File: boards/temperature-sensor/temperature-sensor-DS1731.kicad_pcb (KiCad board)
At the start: 2 copper layers, 20.3 x 17.3 mm, 8 parts, among them J1 CONN_01X04_MALE, M3 MountingHole_3.2mm_M3, U1 DS1731U

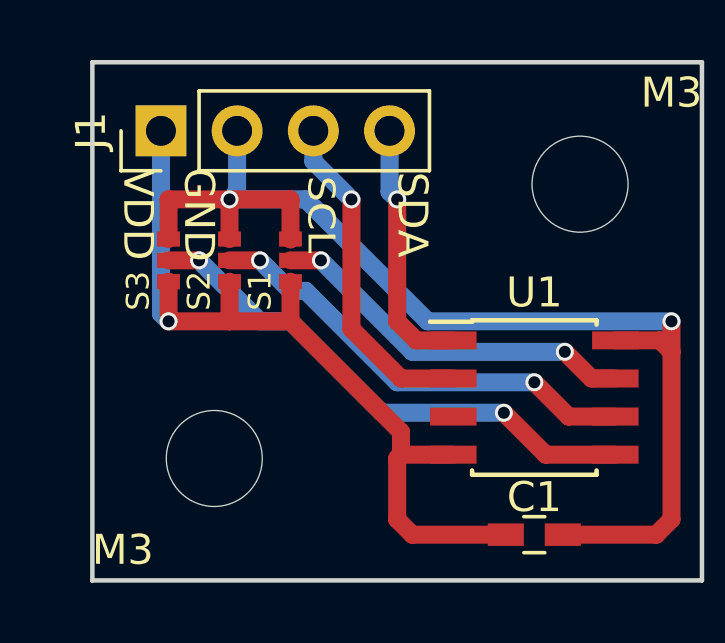
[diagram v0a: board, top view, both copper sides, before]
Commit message: boards/temperature_sensor: reduced number of vias, corrected spelling error
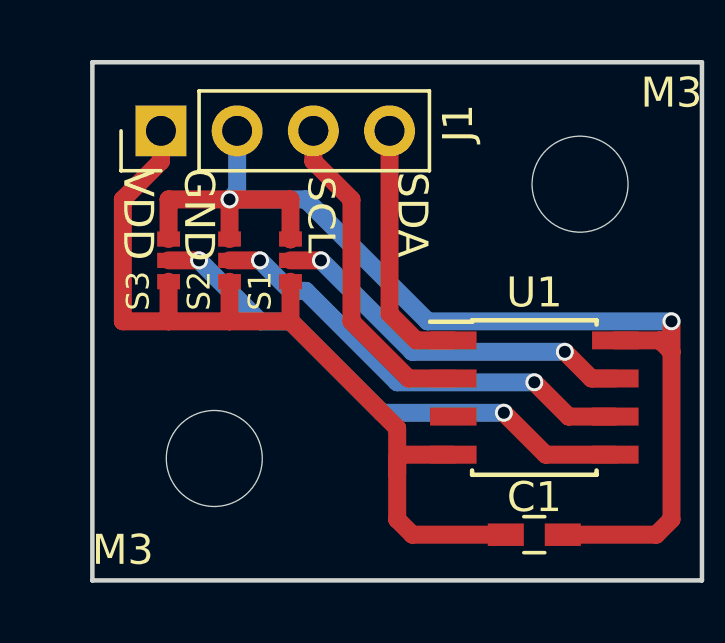
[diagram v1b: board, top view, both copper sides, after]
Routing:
- net /GND: track 28.2 -> 30.8 mm, vias 1 -> 0
- net /SCL: track 11.2 -> 11.1 mm, vias 1 -> 0
- net /SDA: vias 1 -> 0
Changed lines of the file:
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@@
     (thickness 1.6)
     (drawings 12)
-    (tracks 70)
+    (tracks 68)
     (zones 0)
     (modules 8)
@@
     (34 B.Paste user)
     (35 F.Paste user)
-    (36 B.SilkS user)
-    (37 F.SilkS user)
+    (36 B.SilkS user hide)
+    (37 F.SilkS user hide)
     (38 B.Mask user)
     (39 F.Mask user)
@@
     (descr "Through hole straight pin header, 1x04, 2.54mm pitch, single row")
     (tags "Through hole pin header THT 1x04 2.54mm single row")
-    (fp_text reference J1 (at 0 -2.33 90) (layer F.SilkS)
+    (fp_text reference J1 (at 0.254 9.906 90) (layer F.SilkS)
       (effects (font (size 1 1) (thickness 0.15)))
     )
@@
     (effects (font (size 1 1) (thickness 0.2)))
   )
+  (segment (start 128.27 104.902) (end 128.27 102.87) (width 0.6) (layer B.Cu) (net 1))
+  (segment (start 128.016 105.156) (end 128.27 104.902) (width 0.6) (layer B.Cu) (net 1))
   (segment (start 128.016 105.156) (end 130.556 105.156) (width 0.6) (layer B.Cu) (net 1))
   (segment (start 142.748 109.22) (end 142.748 110.236) (width 0.6) (layer F.Cu) (net 1))
@@
   (segment (start 130.556 105.156) (end 134.62 109.22) (width 0.6) (layer B.Cu) (net 1))
   (segment (start 128.016 106.4768) (end 128.016 105.156) (width 0.6) (layer F.Cu) (net 1))
-  (segment (start 128.27 104.902) (end 128.27 102.87) (width 0.6) (layer B.Cu) (net 1))
-  (segment (start 128.016 105.156) (end 128.27 104.902) (width 0.6) (layer B.Cu) (net 1))
   (via (at 128.016 105.156) (size 0.6) (drill 0.4) (layers F.Cu B.Cu) (net 1))
   (segment (start 125.984 106.4768) (end 125.984 105.156) (width 0.6) (layer F.Cu) (net 1))
@@
   (segment (start 142.748 110.236) (end 142.748 115.824) (width 0.6) (layer F.Cu) (net 1))
   (segment (start 142.748 115.824) (end 142.24 116.332) (width 0.6) (layer F.Cu) (net 1))
-  (via (at 125.984 109.22) (size 0.6) (drill 0.4) (layers F.Cu B.Cu) (net 2))
-  (segment (start 125.73 102.87) (end 125.73 108.966) (width 0.6) (layer B.Cu) (net 2))
-  (segment (start 125.73 108.966) (end 125.984 109.22) (width 0.6) (layer B.Cu) (net 2))
+  (segment (start 125.73 102.87) (end 125.73 103.886) (width 0.6) (layer F.Cu) (net 2) (status 400000))
+  (segment (start 124.46 109.22) (end 125.984 109.22) (width 0.6) (layer F.Cu) (net 2))
+  (segment (start 124.46 105.156) (end 124.46 109.22) (width 0.6) (layer F.Cu) (net 2))
+  (segment (start 125.73 103.886) (end 124.46 105.156) (width 0.6) (layer F.Cu) (net 2))
+  (segment (start 133.604 114.3) (end 133.604 112.776) (width 0.6) (layer F.Cu) (net 2))
+  (segment (start 133.604 112.776) (end 130.048 109.22) (width 0.6) (layer F.Cu) (net 2))
   (segment (start 128.016 107.8992) (end 128.016 109.22) (width 0.6) (layer F.Cu) (net 2))
   (segment (start 130.048 109.22) (end 128.016 109.22) (width 0.6) (layer F.Cu) (net 2))
   (segment (start 128.016 109.22) (end 125.984 109.22) (width 0.6) (layer F.Cu) (net 2))
   (segment (start 125.984 109.22) (end 125.984 107.8992) (width 0.6) (layer F.Cu) (net 2))
-  (segment (start 133.731 113.665) (end 133.731 112.903) (width 0.6) (layer F.Cu) (net 2))
   (segment (start 130.048 109.22) (end 130.048 107.8992) (width 0.6) (layer F.Cu) (net 2))
-  (segment (start 133.731 112.903) (end 130.048 109.22) (width 0.6) (layer F.Cu) (net 2))
   (segment (start 135.476 113.665) (end 133.731 113.665) (width 0.6) (layer F.Cu) (net 2))
   (segment (start 134.112 116.332) (end 137.226 116.332) (width 0.6) (layer F.Cu) (net 2))
   (segment (start 133.604 115.824) (end 134.112 116.332) (width 0.6) (layer F.Cu) (net 2))
-  (segment (start 133.604 113.792) (end 133.604 115.824) (width 0.6) (layer F.Cu) (net 2))
+  (segment (start 133.604 113.792) (end 133.604 114.3) (width 0.6) (layer F.Cu) (net 2))
+  (segment (start 133.604 114.3) (end 133.604 115.824) (width 0.6) (layer F.Cu) (net 2))
   (segment (start 133.731 113.665) (end 133.604 113.792) (width 0.6) (layer F.Cu) (net 2))
-  (segment (start 133.35 102.87) (end 133.35 104.902) (width 0.6) (layer B.Cu) (net 3))
-  (segment (start 134.239 109.855) (end 135.476 109.855) (width 0.6) (layer F.Cu) (net 3))
-  (segment (start 133.604 109.22) (end 134.239 109.855) (width 0.6) (layer F.Cu) (net 3))
-  (segment (start 133.604 105.156) (end 133.604 109.22) (width 0.6) (layer F.Cu) (net 3))
-  (via (at 133.604 105.156) (size 0.6) (drill 0.4) (layers F.Cu B.Cu) (net 3))
-  (segment (start 133.35 104.902) (end 133.604 105.156) (width 0.6) (layer B.Cu) (net 3))
-  (segment (start 135.476 111.125) (end 133.731 111.125) (width 0.6) (layer F.Cu) (net 4))
-  (segment (start 130.81 103.886) (end 130.81 102.87) (width 0.6) (layer B.Cu) (net 4))
-  (segment (start 132.08 105.156) (end 130.81 103.886) (width 0.6) (layer B.Cu) (net 4))
-  (via (at 132.08 105.156) (size 0.6) (drill 0.4) (layers F.Cu B.Cu) (net 4))
-  (segment (start 132.08 109.474) (end 132.08 105.156) (width 0.6) (layer F.Cu) (net 4))
-  (segment (start 133.731 111.125) (end 132.08 109.474) (width 0.6) (layer F.Cu) (net 4))
+  (segment (start 133.35 102.87) (end 133.35 108.966) (width 0.6) (layer F.Cu) (net 3) (status 400000))
+  (segment (start 134.239 109.855) (end 135.476 109.855) (width 0.6) (layer F.Cu) (net 3) (status 800000))
+  (segment (start 133.35 108.966) (end 134.239 109.855) (width 0.6) (layer F.Cu) (net 3))
+  (segment (start 130.81 102.87) (end 130.81 103.886) (width 0.6) (layer F.Cu) (net 4) (status 400000))
+  (segment (start 133.985 111.125) (end 135.476 111.125) (width 0.6) (layer F.Cu) (net 4) (status 800000))
+  (segment (start 132.08 109.22) (end 133.985 111.125) (width 0.6) (layer F.Cu) (net 4))
+  (segment (start 132.08 105.156) (end 132.08 109.22) (width 0.6) (layer F.Cu) (net 4))
+  (segment (start 130.81 103.886) (end 132.08 105.156) (width 0.6) (layer F.Cu) (net 4))
   (segment (start 130.048 107.188) (end 131.064 107.188) (width 0.6) (layer F.Cu) (net 6))
   (segment (start 140.081 111.125) (end 140.876 111.125) (width 0.6) (layer F.Cu) (net 6))

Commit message: [docs] export all board layouts
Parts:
- moved J1 90.3 mm to (61.0, 40.0)
- moved C1 90.3 mm to (73.4, 53.5)
- moved M3 90.3 mm to (62.7, 50.9)
- moved M3 90.3 mm to (74.9, 41.8)
- moved S1 90.3 mm to (65.3, 44.3)
- moved S2 90.3 mm to (63.2, 44.3)
- moved S3 90.3 mm to (61.2, 44.3)
- moved U1 90.3 mm to (73.4, 48.9)

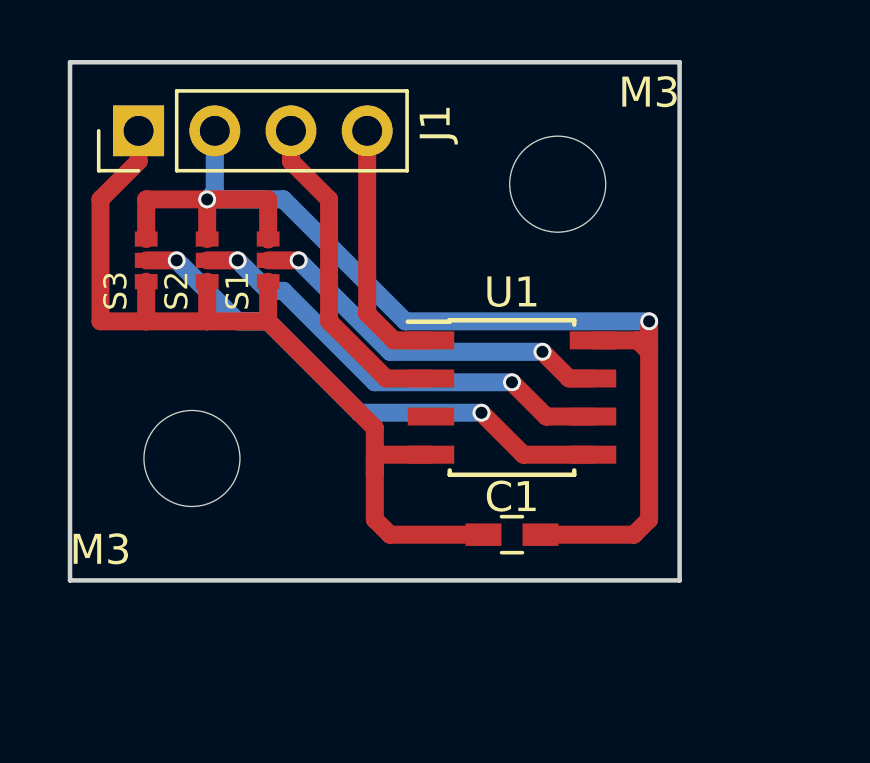
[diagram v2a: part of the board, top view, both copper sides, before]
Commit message: fix/ds1731: updated footprint and dimensions, pls check footprint
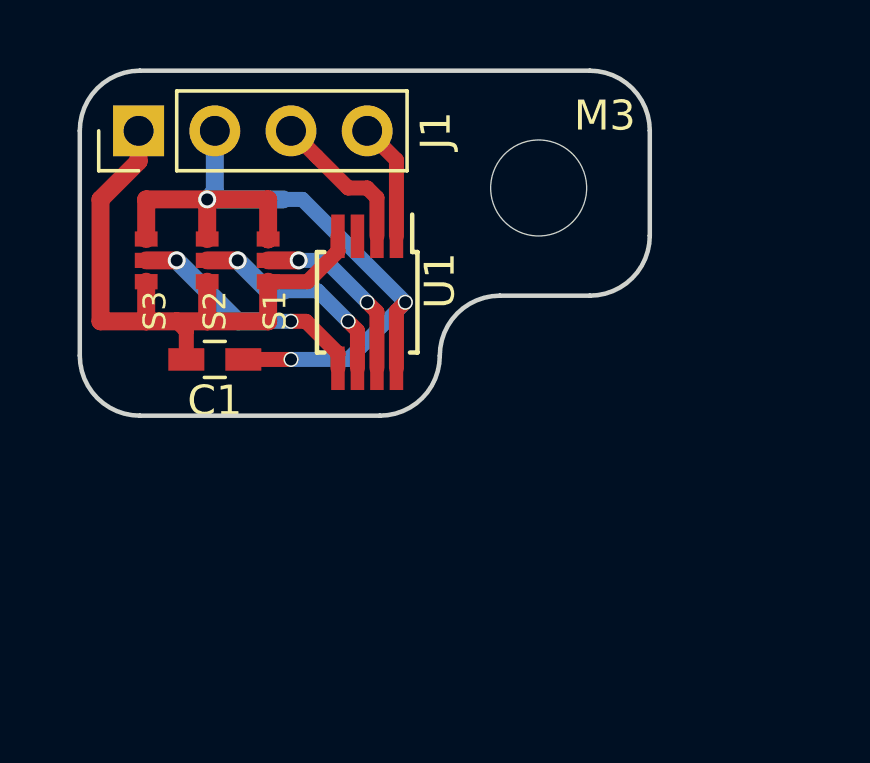
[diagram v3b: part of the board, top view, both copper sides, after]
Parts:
- removed the M3 at (62.7, 50.9)
- U1: footprint Housings_SOIC:SOIC-8-1EP_3.9x4.9mm_Pitch1.27mm -> Housings_SSOP:MSOP-8_3x3mm_Pitch0.65mm
- moved C1 11.5 mm to (63.5, 47.6)
- moved U1 5.78 mm to (68.6, 45.7), turned to 270 degrees
- moved M3 0.65 mm to (74.3, 41.9)
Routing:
- net /VDD: track 39.3 -> 27.0 mm, vias 2 -> 3
- net /GND: track 30.8 -> 21.1 mm
- net Net-(S3-Pad2): track 17.6 -> 8.17 mm
- net Net-(S2-Pad2): track 15.0 -> 7.23 mm
- net Net-(S1-Pad2): track 12.5 -> 6.22 mm
- net /SCL: track 11.1 -> 5.07 mm
- net /SDA: track 8.59 -> 3.92 mm
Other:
- board size 20.3 x 17.3 mm -> 19 x 11.5 mm
- net class Default: trace_width 0.6 -> 0.5; via_dia 0.6 -> 0.5

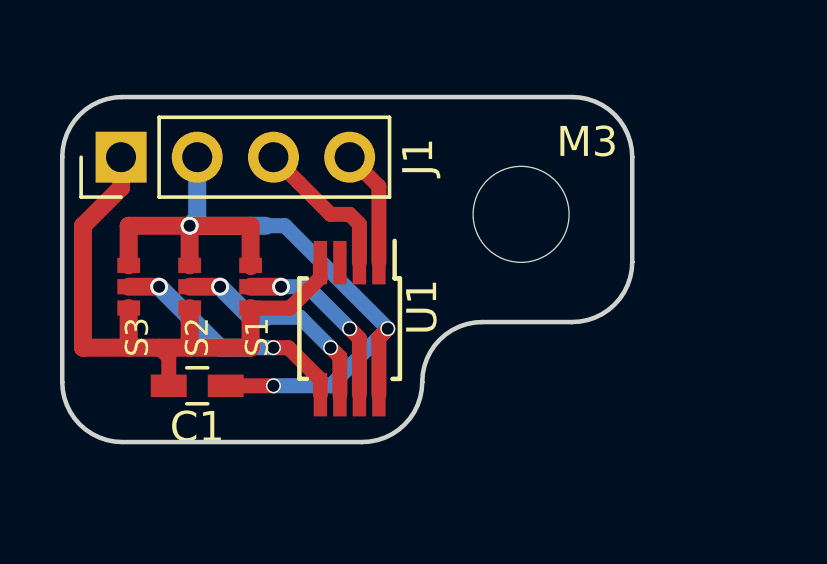
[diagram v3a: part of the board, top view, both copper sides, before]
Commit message: fix/ds1731: changed mounting hole to m2
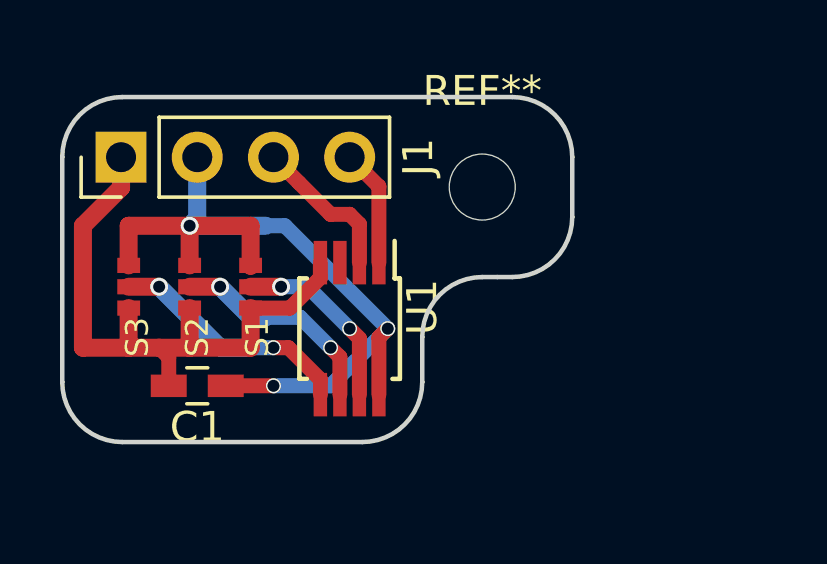
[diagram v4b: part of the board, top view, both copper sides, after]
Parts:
- removed M3: MountingHole_3.2mm_M3, Mounting_Holes:MountingHole_3.2mm_M3
- added REF**: MountingHole_2.2mm_M2, Mounting_Holes:MountingHole_2.2mm_M2, F.Cu at (73.0, 41.0)
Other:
- board size 19 x 11.5 mm -> 17 x 11.5 mm
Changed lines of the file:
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@@
 (kicad_pcb (version 4) (host pcbnew 4.0.7-e2-6376~58~ubuntu16.04.1)
   (general
-    (links 15)
-    (no_connects 8)
-    (area 44.328571 33.8 143.294857 118.05)
+    (links 0)
+    (no_connects 1)
+    (area 58.924999 37.924999 76.075001 49.575001)
     (thickness 1.6)
-    (drawings 21)
+    (drawings 23)
     (tracks 65)
     (zones 0)
@@
     )
   )
-  (module Mounting_Holes:MountingHole_3.2mm_M3 (layer F.Cu)
-    (at 74.295 41.91)
-    (descr "Mounting Hole 3.2mm, no annular, M3")
-    (tags "mounting hole 3.2mm no annular m3")
-    (fp_text reference M3 (at 2.205 -2.41) (layer F.SilkS)
-      (effects (font (size 1 1) (thickness 0.15)))
-    )
-    (fp_text value MountingHole_3.2mm_M3 (at 28.705 -0.91) (layer F.Fab)
-      (effects (font (size 1 1) (thickness 0.15)))
-    )
-    (fp_circle (center 0 0) (end 3.2 0) (layer Cmts.User) (width 0.15))
-    (fp_circle (center 0 0) (end 3.45 0) (layer F.CrtYd) (width 0.05))
-    (pad 1 np_thru_hole circle (at 0 0) (size 3.2 3.2) (drill 3.2) (layers *.Cu *.Mask))
-  )
   (module Capacitors_SMD:C_0603_HandSoldering (layer F.Cu)
     (at 63.5 47.625)
@@
     )
   )
-  (dimension 7.5 (width 0.3) (layer Cmts.User)
-    (gr_text "7.500 mm" (at 80.85 41.75 270) (layer Cmts.User)
+  (module Mounting_Holes:MountingHole_2.2mm_M2 (layer F.Cu)
+    (at 73 41)
+    (descr "Mounting Hole 2.2mm, no annular, M2")
+    (tags "mounting hole 2.2mm no annular m2")
+    (fp_text reference REF** (at 0 -3.2) (layer F.SilkS)
+      (effects (font (size 1 1) (thickness 0.15)))
+    )
+    (fp_text value MountingHole_2.2mm_M2 (at 0 3.2) (layer F.Fab)
+      (effects (font (size 1 1) (thickness 0.15)))
+    )
+    (fp_circle (center 0 0) (end 2.2 0) (layer Cmts.User) (width 0.15))
+    (fp_circle (center 0 0) (end 2.45 0) (layer F.CrtYd) (width 0.05))
+    (pad 1 np_thru_hole circle (at 0 0) (size 2.2 2.2) (drill 2.2) (layers *.Cu *.Mask))
+  )
+  (gr_line (start 71 46) (end 71 47.5) (layer Edge.Cuts) (width 0.15))
+  (gr_line (start 73.5 44) (end 73 44) (layer Edge.Cuts) (width 0.15))
+  (gr_line (start 74 44) (end 73.5 44) (layer Edge.Cuts) (width 0.15))
+  (gr_line (start 76 40) (end 76 42) (layer Edge.Cuts) (width 0.15))
+  (gr_line (start 61 38) (end 74 38) (layer Edge.Cuts) (width 0.15))
+  (gr_arc (start 74 40) (end 74 38) (angle 90) (layer Edge.Cuts) (width 0.15))
+  (gr_arc (start 74 42) (end 76 42) (angle 90) (layer Edge.Cuts) (width 0.15))
+  (gr_arc (start 73 46) (end 71 46) (angle 90) (layer Edge.Cuts) (width 0.15))
+  (dimension 6 (width 0.3) (layer Cmts.User)
+    (gr_text "6.000 mm" (at 78.85 41 270) (layer Cmts.User)
       (effects (font (size 1.5 1.5) (thickness 0.3)))
     )
-    (feature1 (pts (xy 78.5 45.5) (xy 82.2 45.5)))
-    (feature2 (pts (xy 78.5 38) (xy 82.2 38)))
-    (crossbar (pts (xy 79.5 38) (xy 79.5 45.5)))
-    (arrow1a (pts (xy 79.5 45.5) (xy 78.913579 44.373496)))
-    (arrow1b (pts (xy 79.5 45.5) (xy 80.086421 44.373496)))
-    (arrow2a (pts (xy 79.5 38) (xy 78.913579 39.126504)))
-    (arrow2b (pts (xy 79.5 38) (xy 80.086421 39.126504)))
-  )
-  (dimension 19 (width 0.3) (layer Cmts.User)
-    (gr_text "19.000 mm" (at 68.5 35.15) (layer Cmts.User)
+    (feature1 (pts (xy 76.5 44) (xy 80.2 44)))
+    (feature2 (pts (xy 76.5 38) (xy 80.2 38)))
+    (crossbar (pts (xy 77.5 38) (xy 77.5 44)))
+    (arrow1a (pts (xy 77.5 44) (xy 76.913579 42.873496)))
+    (arrow1b (pts (xy 77.5 44) (xy 78.086421 42.873496)))
+    (arrow2a (pts (xy 77.5 38) (xy 76.913579 39.126504)))
+    (arrow2b (pts (xy 77.5 38) (xy 78.086421 39.126504)))
+  )
+  (dimension 17 (width 0.3) (layer Cmts.User)
+    (gr_text "17.000 mm" (at 67.5 34.65) (layer Cmts.User)
       (effects (font (size 1.5 1.5) (thickness 0.3)))
     )
-    (feature1 (pts (xy 78 37.5) (xy 78 33.8)))
-    (feature2 (pts (xy 59 37.5) (xy 59 33.8)))
-    (crossbar (pts (xy 59 36.5) (xy 78 36.5)))
-    (arrow1a (pts (xy 78 36.5) (xy 76.873496 37.086421)))
-    (arrow1b (pts (xy 78 36.5) (xy 76.873496 35.913579)))
-    (arrow2a (pts (xy 59 36.5) (xy 60.126504 37.086421)))
-    (arrow2b (pts (xy 59 36.5) (xy 60.126504 35.913579)))
+    (feature1 (pts (xy 76 37.5) (xy 76 33.3)))
+    (feature2 (pts (xy 59 37.5) (xy 59 33.3)))
+    (crossbar (pts (xy 59 36) (xy 76 36)))
+    (arrow1a (pts (xy 76 36) (xy 74.873496 36.586421)))
+    (arrow1b (pts (xy 76 36) (xy 74.873496 35.413579)))
+    (arrow2a (pts (xy 59 36) (xy 60.126504 36.586421)))
+    (arrow2b (pts (xy 59 36) (xy 60.126504 35.413579)))
   )
   (dimension 11.5 (width 0.3) (layer Cmts.User)
@@
     (arrow2b (pts (xy 59 51) (xy 60.126504 50.413579)))
   )
-  (gr_line (start 76 38) (end 61 38) (layer Edge.Cuts) (width 0.15))
   (gr_line (start 69 49.5) (end 61 49.5) (layer Edge.Cuts) (width 0.15))
-  (gr_line (start 78 43.5) (end 78 40) (layer Edge.Cuts) (width 0.15))
-  (gr_line (start 73 45.5) (end 76 45.5) (layer Edge.Cuts) (width 0.15))
-  (gr_arc (start 76 43.5) (end 78 43.5) (angle 90) (layer Edge.Cuts) (width 0.15))
-  (gr_arc (start 73 47.5) (end 71 47.5) (angle 90) (layer Edge.Cuts) (width 0.15))
   (gr_arc (start 69 47.5) (end 71 47.5) (angle 90) (layer Edge.Cuts) (width 0.15))
-  (gr_arc (start 76 40) (end 76 38) (angle 90) (layer Edge.Cuts) (width 0.15))
   (gr_line (start 59 47.5) (end 59 40) (layer Edge.Cuts) (width 0.15))
   (gr_arc (start 61 40) (end 59 40) (angle 90) (layer Edge.Cuts) (width 0.15))

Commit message: [temperature-sensor] export gerber for second revision
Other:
- rule pad_to_mask_clearance: 0.2 -> 0.05
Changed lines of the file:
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@@
-(kicad_pcb (version 4) (host pcbnew 4.0.7-e2-6376~58~ubuntu16.04.1)
+(kicad_pcb (version 4) (host pcbnew 4.0.6)
   (general
-    (links 0)
+    (links 15)
     (no_connects 1)
-    (area 58.924999 37.924999 76.075001 49.575001)
+    (area 44.328571 33.3 143.294857 118.05)
     (thickness 1.6)
     (drawings 23)
@@
     (pad_size 0.508 0.762)
     (pad_drill 0)
-    (pad_to_mask_clearance 0.2)
+    (pad_to_mask_clearance 0.05)
     (aux_axis_origin 0 0)
     (visible_elements 7FFFFFFF)
     (pcbplotparams
-      (layerselection 0x01030_80000001)
-      (usegerberextensions false)
-      (excludeedgelayer false)
+      (layerselection 0x010f0_80000001)
+      (usegerberextensions true)
+      (excludeedgelayer true)
       (linewidth 0.100000)
       (plotframeref false)
@@
       (padsonsilk false)
       (subtractmaskfromsilk false)
-      (outputformat 4)
+      (outputformat 1)
       (mirror false)
       (drillshape 0)
       (scaleselection 1)
-      (outputdirectory ""))
+      (outputdirectory gerber/))
   )
   (net 0 "")
